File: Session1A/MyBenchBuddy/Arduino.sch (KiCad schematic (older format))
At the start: 0 parts

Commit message: Understanding the Arduino Module
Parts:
- added ARD?: ARDUINOPINS, ~, symbol ARDUINOPINS
- added R? (x13): R, ~, symbol R
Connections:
- net MISO: now also R?.2
- net MOSI: now also R?.2
- net SCLK: now also R?.2
- net TACH_MEAS: now also R?.1
- new net: ARD?.11 (Digital0), R?.1
- new net: ARD?.12 (Digital1), R?.1
- new net: ARD?.19 (Digital8), R?.1
- new net: ARD?.20 (PWM0), R?.1
- new net: ARD?.21 (CS_N), R?.1
- new net: ARD?.22 (MOSI), R?.1
- new net: ARD?.23 (MISO), R?.1
- new net: ARD?.24 (SCK), R?.1
- new net: ARD?.5 (AnalogIn0), R?.2
- new net: ARD?.6 (AnalogIn1), R?.2
- new net: ARD?.7 (AnalogIn2), R?.2
- new net: ARD?.8 (AnalogIn3), R?.2
- new net ADC_CS_N: R?.2
- new net CURR_MEAS: R?.1
- new net DAC_CS_N: R?.2
- new net FAN_EN_N: R?.2
- new net GND: R?.1
- new net LED_EN_PWM: R?.2
- new net RELAY+: R?.2
- new net RELAY-: R?.2
- new net V+_ADJ_MON: R?.1
- new net V-_ADJ_MON: R?.1

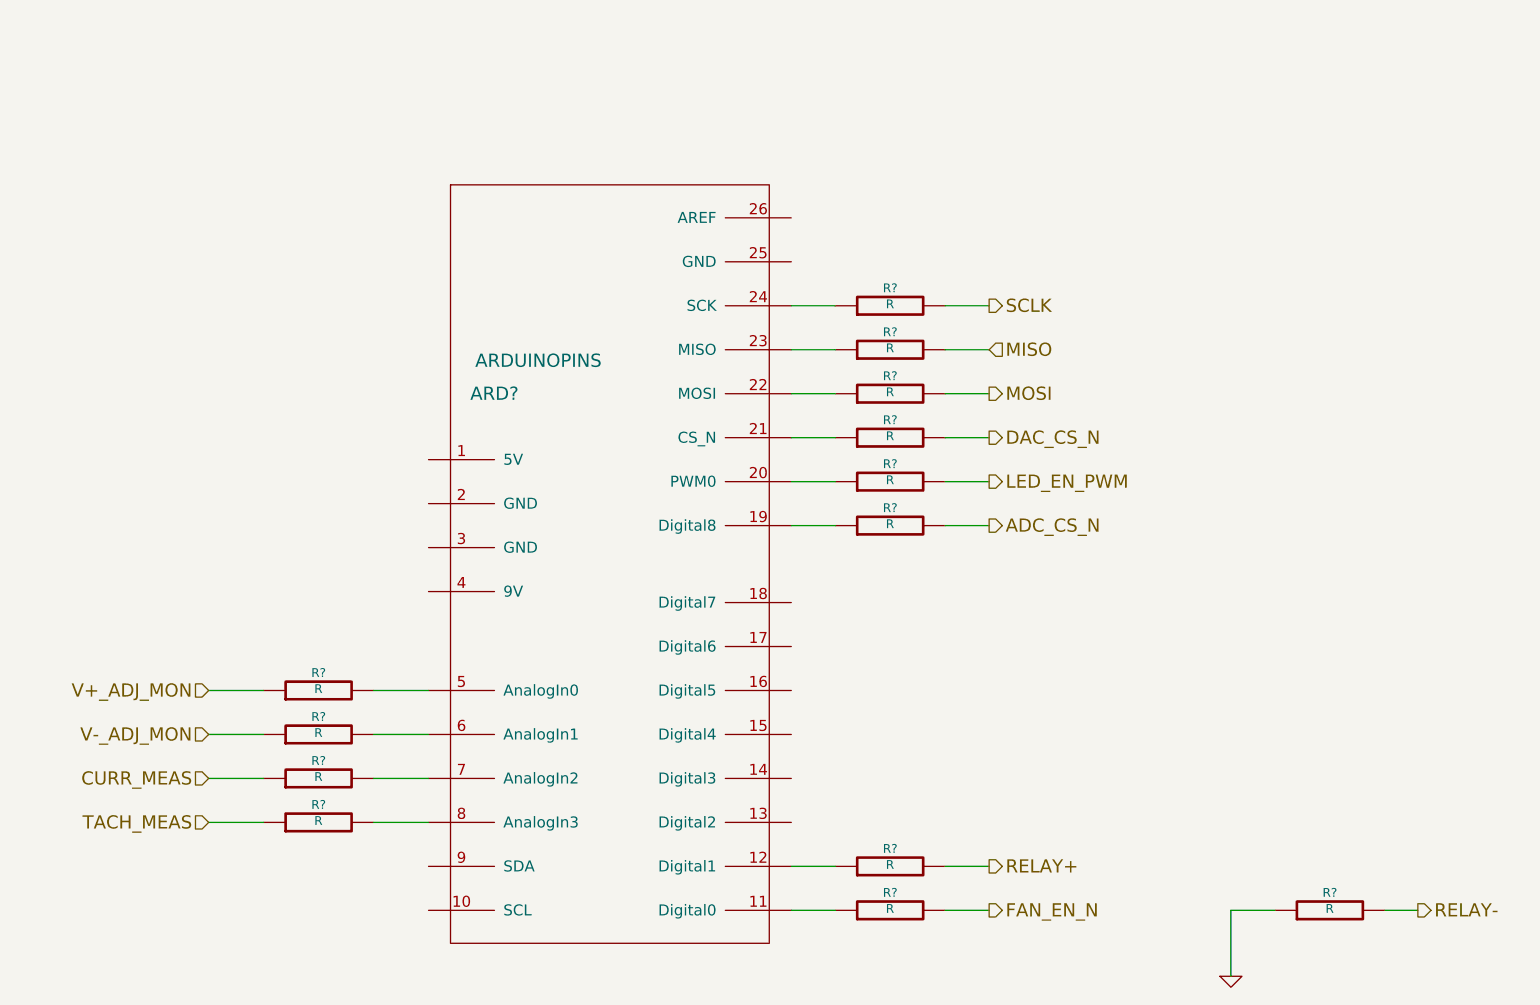
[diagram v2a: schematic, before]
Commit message: Revisiting The Current/Fan Module
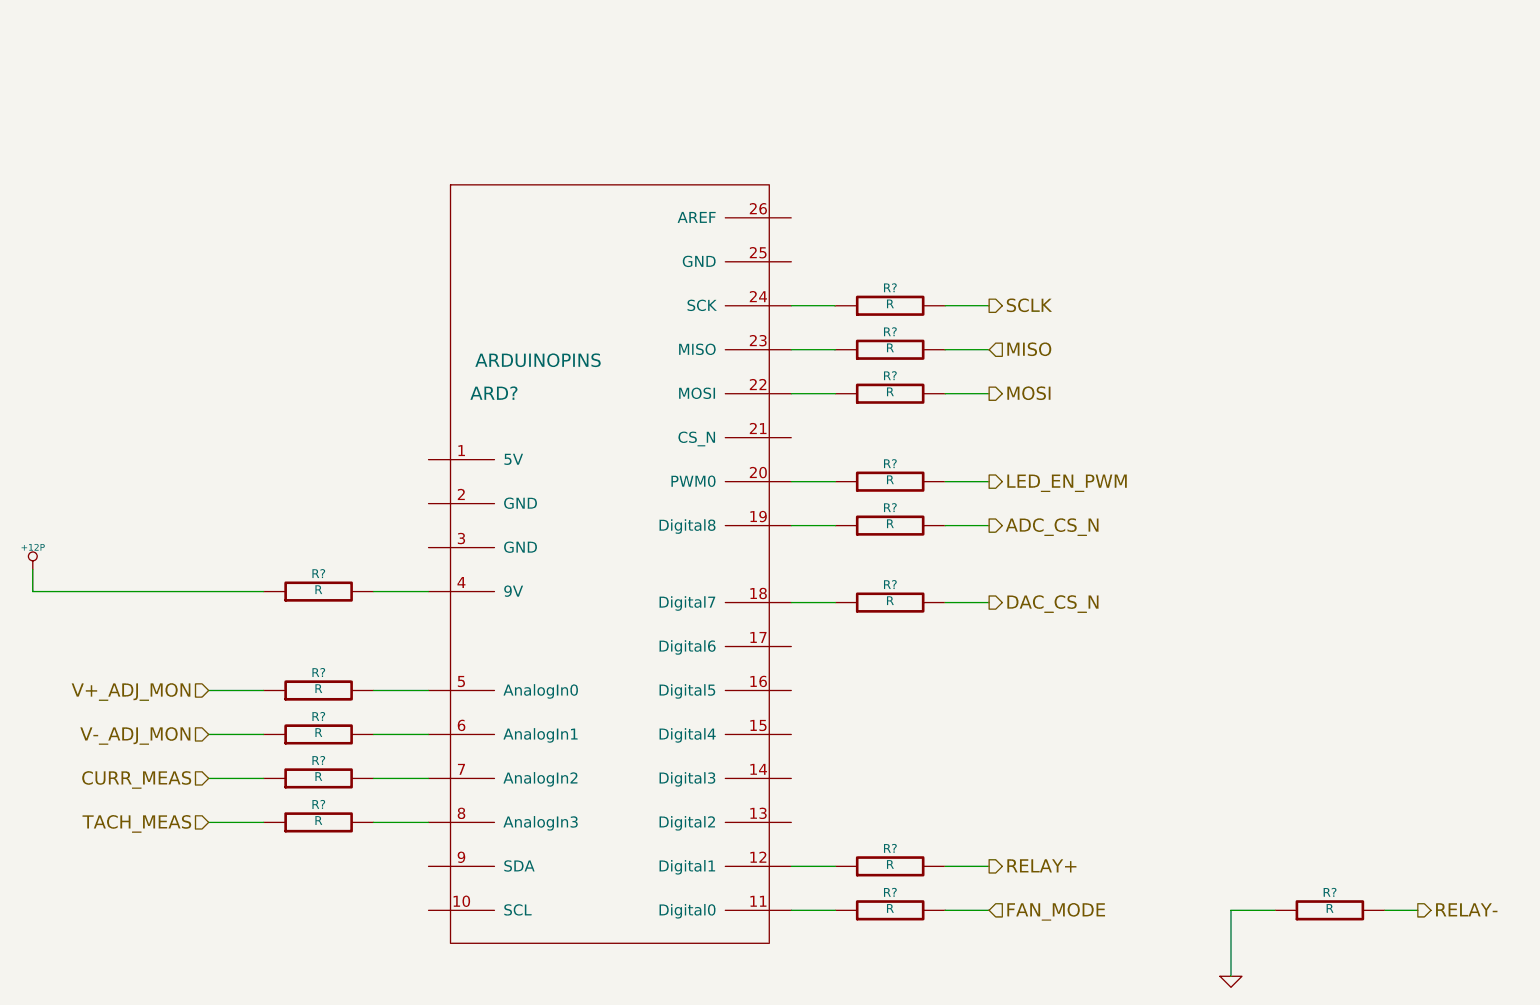
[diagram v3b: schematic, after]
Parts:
- added R?: R, ~, symbol R
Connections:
- net at ARD?.18 (Digital7): now also R?.1
- net at ARD?.21 (CS_N): no longer R?.1
- net at ARD?.4 (9V): now also R?.2
- net FAN_EN_N renamed FAN_MODE
- new net +12P: R?.1
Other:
- moved on the sheet: R?
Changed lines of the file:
@@
 $Descr A4 11693 8268
 encoding utf-8
-Sheet 8 9
+Sheet 7 9
 Title ""
-Date "26 feb 2014"
+Date "1 mar 2014"
 Rev ""
 Comp ""
@@
 Text HLabel 6200 2600 2    60   Output ~ 0
 SCLK
-Text HLabel 6200 3200 2    60   Output ~ 0
+Text HLabel 6200 3950 2    60   Output ~ 0
 DAC_CS_N
-Text HLabel 6200 5350 2    60   Output ~ 0
-FAN_EN_N
+Text HLabel 6200 5350 2    60   Input ~ 0
+FAN_MODE
 Text HLabel 2650 4950 0    60   Input ~ 0
 TACH_MEAS
@@
 L R R?
 U 1 1 530D6FFE
-P 5750 3200
-F 0 "R?" V 5830 3200 40  0000 C CNN
-F 1 "R" V 5757 3201 40  0000 C CNN
-F 2 "~" V 5680 3200 30  0000 C CNN
-F 3 "~" H 5750 3200 30  0000 C CNN
-	1    5750 3200
+P 5750 3950
+F 0 "R?" V 5830 3950 40  0000 C CNN
+F 1 "R" V 5757 3951 40  0000 C CNN
+F 2 "~" V 5680 3950 30  0000 C CNN
+F 3 "~" H 5750 3950 30  0000 C CNN
+	1    5750 3950
 	0    -1   -1   0
 $EndComp
@@
 	5500 3000 5300 3000
 Wire Wire Line
-	5300 3200 5500 3200
-Wire Wire Line
-	6000 3200 6200 3200
+	5300 3950 5500 3950
+Wire Wire Line
+	6000 3950 6200 3950
 Wire Wire Line
 	6200 3000 6000 3000
@@
 Wire Wire Line
 	6000 3600 6200 3600
+$Comp
+L R R?
+U 1 1 531166F5
+P 3150 3900
+F 0 "R?" V 3230 3900 40  0000 C CNN
+F 1 "R" V 3157 3901 40  0000 C CNN
+F 2 "~" V 3080 3900 30  0000 C CNN
+F 3 "~" H 3150 3900 30  0000 C CNN
+	1    3150 3900
+	0    -1   -1   0
+$EndComp
+Wire Wire Line
+	3650 3900 3400 3900
+Wire Wire Line
+	2900 3900 1850 3900
+Wire Wire Line
+	1850 3900 1850 3800
+$Comp
+L +12P #PWR?
+U 1 1 53116736
+P 1850 3800
+F 0 "#PWR?" H 1850 3770 30  0001 C CNN
+F 1 "+12P" H 1850 3900 30  0000 C CNN
+F 2 "" H 1850 3800 60  0000 C CNN
+F 3 "" H 1850 3800 60  0000 C CNN
+	1    1850 3800
+	1    0    0    -1
+$EndComp
 $EndSCHEMATC

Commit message: initial
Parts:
- added R44, R45, R46: R, ~, symbol R
- gave numbers to parts that had none: 15
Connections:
- net at ARD1.15 (Digital4): now also R46.1
- net at ARD1.16 (Digital5): now also R45.1
- net at ARD1.21 (CS_N): now also R44.1
- new net FAN_PWM: R44.2
- new net ~DR: R46.2
- new net ~RESET: R45.2
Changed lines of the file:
@@
 Sheet 7 9
 Title ""
-Date "1 mar 2014"
+Date "15 mar 2014"
 Rev ""
 Comp ""
@@
 TACH_MEAS
 $Comp
-L ARDUINOPINS ARD?
+L ARDUINOPINS ARD1
 U 1 1 530D49AA
 P 4450 3650
-F 0 "ARD?" H 3950 4300 60  0000 C CNN
+F 0 "ARD1" H 3950 4300 60  0000 C CNN
 F 1 "ARDUINOPINS" H 4150 4450 60  0000 C CNN
 F 2 "~" H 2500 3700 60  0000 C CNN
@@
 CURR_MEAS
 $Comp
-L R R?
+L R R33
 U 1 1 530D57E6
 P 5750 5350
-F 0 "R?" V 5830 5350 40  0000 C CNN
+F 0 "R33" V 5830 5350 40  0000 C CNN
 F 1 "R" V 5757 5351 40  0000 C CNN
 F 2 "~" V 5680 5350 30  0000 C CNN
@@
 	6000 5350 6200 5350
 $Comp
-L R R?
+L R R32
 U 1 1 530D6336
 P 5750 5150
-F 0 "R?" V 5830 5150 40  0000 C CNN
+F 0 "R32" V 5830 5150 40  0000 C CNN
 F 1 "R" V 5757 5151 40  0000 C CNN
 F 2 "~" V 5680 5150 30  0000 C CNN
@@
 	7300 5350 7300 5650
 $Comp
-L GND #PWR?
+L GND #PWR41
 U 1 1 530D5D7E
 P 7300 5650
-F 0 "#PWR?" H 7300 5650 30  0001 C CNN
+F 0 "#PWR41" H 7300 5650 30  0001 C CNN
 F 1 "GND" H 7300 5580 30  0001 C CNN
 F 2 "" H 7300 5650 60  0000 C CNN
@@
 $EndComp
 $Comp
-L R R?
+L R R24
 U 1 1 530D5FDE
 P 3150 4750
-F 0 "R?" V 3230 4750 40  0000 C CNN
+F 0 "R24" V 3230 4750 40  0000 C CNN
 F 1 "R" V 3157 4751 40  0000 C CNN
 F 2 "~" V 3080 4750 30  0000 C CNN
@@
 $EndComp
 $Comp
-L R R?
+L R R25
 U 1 1 530D5FEB
 P 3150 4950
-F 0 "R?" V 3230 4950 40  0000 C CNN
+F 0 "R25" V 3230 4950 40  0000 C CNN
 F 1 "R" V 3157 4951 40  0000 C CNN
 F 2 "~" V 3080 4950 30  0000 C CNN
@@
 V-_ADJ_MON
 $Comp
-L R R?
+L R R23
 U 1 1 530D6D63
 P 3150 4550
-F 0 "R?" V 3230 4550 40  0000 C CNN
+F 0 "R23" V 3230 4550 40  0000 C CNN
 F 1 "R" V 3157 4551 40  0000 C CNN
 F 2 "~" V 3080 4550 30  0000 C CNN
@@
 $EndComp
 $Comp
-L R R?
+L R R22
 U 1 1 530D6D69
 P 3150 4350
-F 0 "R?" V 3230 4350 40  0000 C CNN
+F 0 "R22" V 3230 4350 40  0000 C CNN
 F 1 "R" V 3157 4351 40  0000 C CNN
 F 2 "~" V 3080 4350 30  0000 C CNN
@@
 	3650 4350 3400 4350
 $Comp
-L R R?
+L R R31
 U 1 1 530D6FFE
 P 5750 3950
-F 0 "R?" V 5830 3950 40  0000 C CNN
+F 0 "R31" V 5830 3950 40  0000 C CNN
 F 1 "R" V 5757 3951 40  0000 C CNN
 F 2 "~" V 5680 3950 30  0000 C CNN
@@
 $EndComp
 $Comp
-L R R?
+L R R28
 U 1 1 530D7004
 P 5750 3000
-F 0 "R?" V 5830 3000 40  0000 C CNN
+F 0 "R28" V 5830 3000 40  0000 C CNN
 F 1 "R" V 5757 3001 40  0000 C CNN
 F 2 "~" V 5680 3000 30  0000 C CNN
@@
 $EndComp
 $Comp
-L R R?
+L R R27
 U 1 1 530D700A
 P 5750 2800
-F 0 "R?" V 5830 2800 40  0000 C CNN
+F 0 "R27" V 5830 2800 40  0000 C CNN
 F 1 "R" V 5757 2801 40  0000 C CNN
 F 2 "~" V 5680 2800 30  0000 C CNN
@@
 $EndComp
 $Comp
-L R R?
+L R R26
 U 1 1 530D7010
 P 5750 2600
-F 0 "R?" V 5830 2600 40  0000 C CNN
+F 0 "R26" V 5830 2600 40  0000 C CNN
 F 1 "R" V 5757 2601 40  0000 C CNN
 F 2 "~" V 5680 2600 30  0000 C CNN
@@
 	6200 2600 6000 2600
 $Comp
-L R R?
+L R R34
 U 1 1 530D72F3
 P 7750 5350
-F 0 "R?" V 7830 5350 40  0000 C CNN
+F 0 "R34" V 7830 5350 40  0000 C CNN
 F 1 "R" V 7757 5351 40  0000 C CNN
 F 2 "~" V 7680 5350 30  0000 C CNN
@@
 LED_EN_PWM
 $Comp
-L R R?
+L R R29
 U 1 1 530D77C7
 P 5750 3400
-F 0 "R?" V 5830 3400 40  0000 C CNN
+F 0 "R29" V 5830 3400 40  0000 C CNN
 F 1 "R" V 5757 3401 40  0000 C CNN
 F 2 "~" V 5680 3400 30  0000 C CNN
@@
 ADC_CS_N
 $Comp
-L R R?
+L R R30
 U 1 1 530DC972
 P 5750 3600
-F 0 "R?" V 5830 3600 40  0000 C CNN
+F 0 "R30" V 5830 3600 40  0000 C CNN
 F 1 "R" V 5757 3601 40  0000 C CNN
 F 2 "~" V 5680 3600 30  0000 C CNN
@@
 	6000 3600 6200 3600
 $Comp
-L R R?
+L R R21
 U 1 1 531166F5
 P 3150 3900
-F 0 "R?" V 3230 3900 40  0000 C CNN
+F 0 "R21" V 3230 3900 40  0000 C CNN
 F 1 "R" V 3157 3901 40  0000 C CNN
 F 2 "~" V 3080 3900 30  0000 C CNN
@@
 	1850 3900 1850 3800
 $Comp
-L +12P #PWR?
+L +12P #PWR40
 U 1 1 53116736
 P 1850 3800
-F 0 "#PWR?" H 1850 3770 30  0001 C CNN
+F 0 "#PWR40" H 1850 3770 30  0001 C CNN
 F 1 "+12P" H 1850 3900 30  0000 C CNN
 F 2 "" H 1850 3800 60  0000 C CNN
@@
 	1    0    0    -1
 $EndComp
+Text HLabel 6200 4350 2    60   Output ~ 0
+~RESET
+Text HLabel 6200 4550 2    60   Output ~ 0
+~DR
+$Comp
+L R R45
+U 1 1 53208142
+P 5750 4350
+F 0 "R45" V 5830 4350 40  0000 C CNN
+F 1 "R" V 5757 4351 40  0000 C CNN
+F 2 "~" V 5680 4350 30  0000 C CNN
+F 3 "~" H 5750 4350 30  0000 C CNN
+	1    5750 4350
+	0    -1   -1   0
+$EndComp
+Wire Wire Line
+	5300 4350 5500 4350
+Wire Wire Line
+	6000 4350 6200 4350
+$Comp
+L R R46
+U 1 1 5320814B
+P 5750 4550
+F 0 "R46" V 5830 4550 40  0000 C CNN
+F 1 "R" V 5757 4551 40  0000 C CNN
+F 2 "~" V 5680 4550 30  0000 C CNN
+F 3 "~" H 5750 4550 30  0000 C CNN
+	1    5750 4550
+	0    -1   -1   0
+$EndComp
+Wire Wire Line
+	5300 4550 5500 4550
+Wire Wire Line
+	6000 4550 6200 4550
+Text HLabel 6200 3200 2    60   Output ~ 0
+FAN_PWM
+$Comp
+L R R44
+U 1 1 5324A908
+P 5750 3200
+F 0 "R44" V 5830 3200 40  0000 C CNN
+F 1 "R" V 5757 3201 40  0000 C CNN
+F 2 "~" V 5680 3200 30  0000 C CNN
+F 3 "~" H 5750 3200 30  0000 C CNN
+	1    5750 3200
+	0    -1   -1   0
+$EndComp
+Wire Wire Line
+	5500 3200 5300 3200
+Wire Wire Line
+	6000 3200 6200 3200
 $EndSCHEMATC
